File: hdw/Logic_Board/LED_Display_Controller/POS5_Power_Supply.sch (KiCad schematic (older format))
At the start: 15 parts, among them U401 LTC3624DD

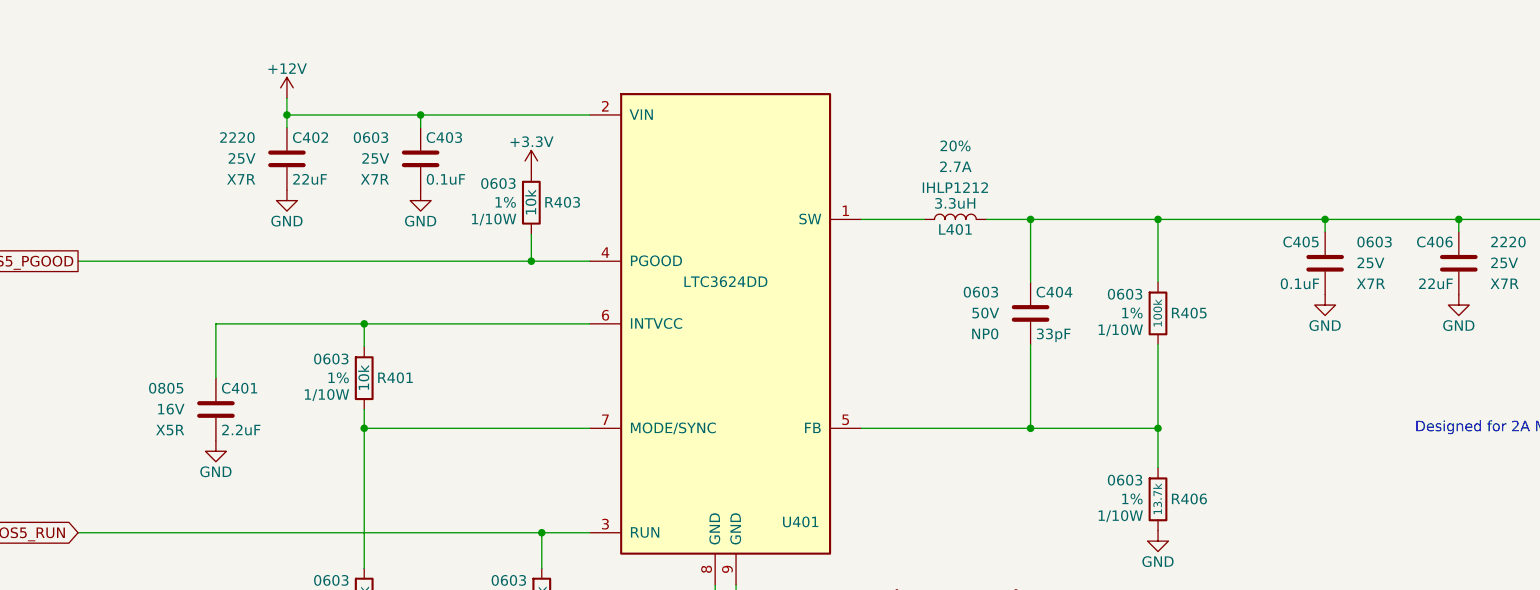
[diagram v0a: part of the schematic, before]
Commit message: Added some digikey partnumbers to components
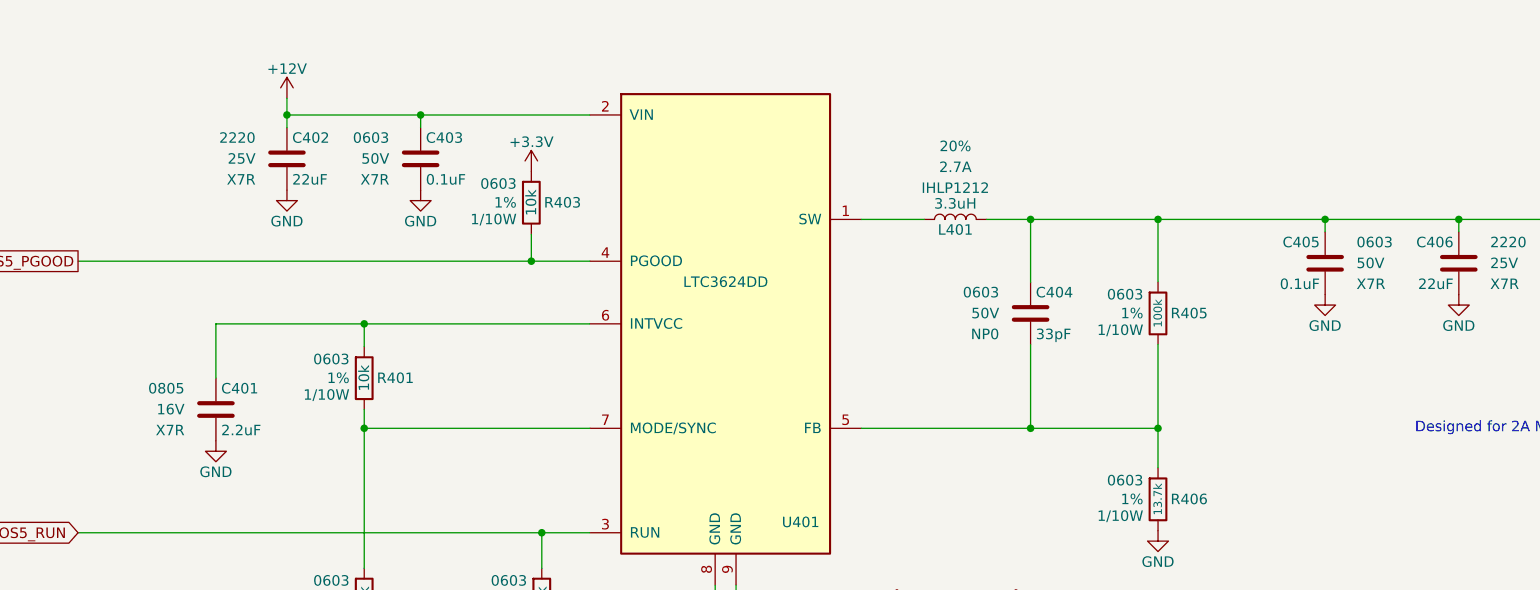
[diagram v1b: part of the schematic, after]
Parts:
- C401: Dielectric X5R -> X7R; Digi-Key PN PN -> 445-5691-1-ND
- C403, C405: footprint (none) -> Capacitors_SMD:C_0603; Digi-Key PN PN -> 311-1344-1-ND; Voltage 25V -> 50V
- C404: Digi-Key PN PN -> 399-1055-1-ND
- L401: Digi-Key PN (none) -> 541-2567-1-ND
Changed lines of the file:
@@
 F 5 "2.7A" V 6290 3230 50  0000 C CNN "Ampacity"
 F 6 "20%" V 6390 3230 50  0000 C CNN "Tolerance"
+F 7 "541-2567-1-ND" H 0   0   50  0001 C CNN "Digi-Key PN"
 	1    6040 3230
 	0    -1   -1   0
@@
 F 5 "50V" H 6250 3680 50  0000 R CNN "Voltage"
 F 6 "NP0" H 6250 3580 50  0000 R CNN "Dielectric"
-F 7 "PN" H 6825 4180 60  0001 C CNN "Digi-Key PN"
+F 7 "399-1055-1-ND" H 6825 4180 60  0001 C CNN "Digi-Key PN"
 	1    6400 3680
 	1    0    0    -1
@@
 F 4 "0805" H 2350 4240 50  0000 R CNN "display_footprint"
 F 5 "16V" H 2350 4140 50  0000 R CNN "Voltage"
-F 6 "X5R" H 2350 4040 50  0000 R CNN "Dielectric"
-F 7 "PN" H 2925 4640 60  0001 C CNN "Digi-Key PN"
+F 6 "X7R" H 2350 4040 50  0000 R CNN "Dielectric"
+F 7 "445-5691-1-ND" H 2925 4640 60  0001 C CNN "Digi-Key PN"
 	1    2500 4140
 	1    0    0    -1
@@
 F 0 "C405" H 7835 3540 50  0000 L CNN
 F 1 "0.1uF" H 7835 3340 50  0000 L CNN
-F 2 "" H 7848 3290 50  0001 C CNN
+F 2 "Capacitors_SMD:C_0603" H 7848 3290 50  0001 C CNN
 F 3 "" H 7835 3540 50  0001 C CNN
 F 4 "0603" H 7660 3540 50  0000 R CNN "display_footprint"
-F 5 "25V" H 7660 3440 50  0000 R CNN "Voltage"
+F 5 "50V" H 7660 3440 50  0000 R CNN "Voltage"
 F 6 "X7R" H 7660 3340 50  0000 R CNN "Dielectric"
-F 7 "PN" H 8235 3940 60  0001 C CNN "Digi-Key PN"
+F 7 "311-1344-1-ND" H 8235 3940 60  0001 C CNN "Digi-Key PN"
 	1    7810 3440
 	-1   0    0    -1
@@
 F 0 "C403" H 3505 3040 50  0000 L CNN
 F 1 "0.1uF" H 3505 2840 50  0000 L CNN
-F 2 "" H 3518 2790 50  0001 C CNN
+F 2 "Capacitors_SMD:C_0603" H 3518 2790 50  0001 C CNN
 F 3 "" H 3505 3040 50  0001 C CNN
 F 4 "0603" H 3330 3040 50  0000 R CNN "display_footprint"
-F 5 "25V" H 3330 2940 50  0000 R CNN "Voltage"
+F 5 "50V" H 3330 2940 50  0000 R CNN "Voltage"
 F 6 "X7R" H 3330 2840 50  0000 R CNN "Dielectric"
-F 7 "PN" H 3905 3440 60  0001 C CNN "Digi-Key PN"
+F 7 "311-1344-1-ND" H 3905 3440 60  0001 C CNN "Digi-Key PN"
 	1    3480 2940
 	1    0    0    -1

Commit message: Finished first pass of digikey part numbers
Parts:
- R401, R402, R403, R404: Digi-Key PN PN -> RMCF0603FT10K0CT-ND
- R405: Digi-Key PN PN -> A106046CT-ND
- R406: Digi-Key PN PN -> P13.7KHCT-ND
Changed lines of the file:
@@
 F 5 "1%" H 7080 3680 50  0000 L CNN "Tolerance"
 F 6 "1/10W" H 7080 3600 50  0000 L CNN "Wattage"
-F 7 "PN" H 7310 4080 60  0001 C CNN "Digi-Key PN"
+F 7 "A106046CT-ND" H 7310 4080 60  0001 C CNN "Digi-Key PN"
 	1    7010 3680
 	-1   0    0    -1
@@
 F 5 "1%" H 3280 3990 50  0000 L CNN "Tolerance"
 F 6 "1/10W" H 3280 3910 50  0000 L CNN "Wattage"
-F 7 "PN" H 3510 4390 60  0001 C CNN "Digi-Key PN"
+F 7 "RMCF0603FT10K0CT-ND" H 3510 4390 60  0001 C CNN "Digi-Key PN"
 	1    3210 3990
 	-1   0    0    -1
@@
 F 5 "1%" H 3280 5050 50  0000 L CNN "Tolerance"
 F 6 "1/10W" H 3280 4970 50  0000 L CNN "Wattage"
-F 7 "PN" H 3510 5450 60  0001 C CNN "Digi-Key PN"
+F 7 "RMCF0603FT10K0CT-ND" H 3510 5450 60  0001 C CNN "Digi-Key PN"
 	1    3210 5050
 	-1   0    0    -1
@@
 F 5 "1%" H 4130 5050 50  0000 L CNN "Tolerance"
 F 6 "1/10W" H 4130 4970 50  0000 L CNN "Wattage"
-F 7 "PN" H 4360 5450 60  0001 C CNN "Digi-Key PN"
+F 7 "RMCF0603FT10K0CT-ND" H 4360 5450 60  0001 C CNN "Digi-Key PN"
 	1    4060 5050
 	-1   0    0    -1
@@
 F 5 "1%" H 4080 3150 50  0000 L CNN "Tolerance"
 F 6 "1/10W" H 4080 3070 50  0000 L CNN "Wattage"
-F 7 "PN" H 4310 3550 60  0001 C CNN "Digi-Key PN"
+F 7 "RMCF0603FT10K0CT-ND" H 4310 3550 60  0001 C CNN "Digi-Key PN"
 	1    4010 3150
 	-1   0    0    -1
@@
 F 5 "1%" H 7080 4570 50  0000 L CNN "Tolerance"
 F 6 "1/10W" H 7080 4490 50  0000 L CNN "Wattage"
-F 7 "PN" H 7310 4970 60  0001 C CNN "Digi-Key PN"
+F 7 "P13.7KHCT-ND" H 7310 4970 60  0001 C CNN "Digi-Key PN"
 	1    7010 4570
 	-1   0    0    -1

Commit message: First pass assignment of footprints to all components
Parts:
- C401: footprint (none) -> Capacitors_SMD:C_0805
- C402, C406, C407: footprint (none) -> Capacitors_SMD:C_2220
- C404: footprint (none) -> Capacitors_SMD:C_0603
- L401: footprint (none) -> Inductors_SMD:L_Vishay_IHLP-1212
- R401, R402, R403, R404, R405, R406: footprint (none) -> Resistors_SMD:R_0603
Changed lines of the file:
@@
 F 0 "L401" V 5990 3230 50  0000 C CNN
 F 1 "3.3uH" V 6115 3230 50  0000 C CNN
-F 2 "" H 6040 3230 50  0001 C CNN
+F 2 "Inductors_SMD:L_Vishay_IHLP-1212" H 6040 3230 50  0001 C CNN
 F 3 "" H 6040 3230 50  0001 C CNN
 F 4 "IHLP1212" V 6190 3230 50  0000 C CNN "display_footprint"
@@
 F 0 "C404" H 6425 3780 50  0000 L CNN
 F 1 "33pF" H 6425 3580 50  0000 L CNN
-F 2 "" H 6438 3530 50  0001 C CNN
+F 2 "Capacitors_SMD:C_0603" H 6438 3530 50  0001 C CNN
 F 3 "" H 6425 3780 50  0001 C CNN
 F 4 "0603" H 6250 3780 50  0000 R CNN "display_footprint"
@@
 F 0 "R405" H 6950 3680 50  0000 R CNN
 F 1 "100k" V 7010 3680 40  0000 C CNN
-F 2 "" H 7010 3680 50  0001 C CNN
+F 2 "Resistors_SMD:R_0603" H 7010 3680 50  0001 C CNN
 F 3 "" H 7010 3680 50  0001 C CNN
 F 4 "0603" H 7080 3770 50  0000 L CNN "display_footprint"
@@
 F 0 "R401" H 3150 3990 50  0000 R CNN
 F 1 "10k" V 3210 3990 50  0000 C CNN
-F 2 "" H 3210 3990 50  0001 C CNN
+F 2 "Resistors_SMD:R_0603" H 3210 3990 50  0001 C CNN
 F 3 "" H 3210 3990 50  0001 C CNN
 F 4 "0603" H 3280 4080 50  0000 L CNN "display_footprint"
@@
 F 0 "R402" H 3150 5050 50  0000 R CNN
 F 1 "10k" V 3210 5050 50  0000 C CNN
-F 2 "" H 3210 5050 50  0001 C CNN
+F 2 "Resistors_SMD:R_0603" H 3210 5050 50  0001 C CNN
 F 3 "" H 3210 5050 50  0001 C CNN
 F 4 "0603" H 3280 5140 50  0000 L CNN "display_footprint"
@@
 F 0 "R404" H 4000 5050 50  0000 R CNN
 F 1 "10k" V 4060 5050 50  0000 C CNN
-F 2 "" H 4060 5050 50  0001 C CNN
+F 2 "Resistors_SMD:R_0603" H 4060 5050 50  0001 C CNN
 F 3 "" H 4060 5050 50  0001 C CNN
 F 4 "0603" H 4130 5140 50  0000 L CNN "display_footprint"
@@
 F 0 "C401" H 2525 4240 50  0000 L CNN
 F 1 "2.2uF" H 2525 4040 50  0000 L CNN
-F 2 "" H 2538 3990 50  0001 C CNN
+F 2 "Capacitors_SMD:C_0805" H 2538 3990 50  0001 C CNN
 F 3 "" H 2525 4240 50  0001 C CNN
 F 4 "0805" H 2350 4240 50  0000 R CNN "display_footprint"
@@
 F 0 "R403" H 3950 3150 50  0000 R CNN
 F 1 "10k" V 4010 3150 50  0000 C CNN
-F 2 "" H 4010 3150 50  0001 C CNN
+F 2 "Resistors_SMD:R_0603" H 4010 3150 50  0001 C CNN
 F 3 "" H 4010 3150 50  0001 C CNN
 F 4 "0603" H 4080 3240 50  0000 L CNN "display_footprint"
@@
 F 0 "C402" H 2865 3040 50  0000 L CNN
 F 1 "22uF" H 2865 2840 50  0000 L CNN
-F 2 "" H 2878 2790 50  0001 C CNN
+F 2 "Capacitors_SMD:C_2220" H 2878 2790 50  0001 C CNN
 F 3 "" H 2865 3040 50  0001 C CNN
 F 4 "445-1453-1-ND" H 3265 3440 60  0001 C CNN "Digi-Key PN"
@@
 F 0 "R406" H 6950 4570 50  0000 R CNN
 F 1 "13.7k" V 7010 4570 40  0000 C CNN
-F 2 "" H 7010 4570 50  0001 C CNN
+F 2 "Resistors_SMD:R_0603" H 7010 4570 50  0001 C CNN
 F 3 "" H 7010 4570 50  0001 C CNN
 F 4 "0603" H 7080 4660 50  0000 L CNN "display_footprint"
@@
 F 0 "C406" H 8475 3540 50  0000 L CNN
 F 1 "22uF" H 8475 3340 50  0000 L CNN
-F 2 "" H 8488 3290 50  0001 C CNN
+F 2 "Capacitors_SMD:C_2220" H 8488 3290 50  0001 C CNN
 F 3 "" H 8475 3540 50  0001 C CNN
 F 4 "445-1453-1-ND" H 8875 3940 60  0001 C CNN "Digi-Key PN"
@@
 F 0 "C407" H 9115 3540 50  0000 L CNN
 F 1 "22uF" H 9115 3340 50  0000 L CNN
-F 2 "" H 9128 3290 50  0001 C CNN
+F 2 "Capacitors_SMD:C_2220" H 9128 3290 50  0001 C CNN
 F 3 "" H 9115 3540 50  0001 C CNN
 F 4 "445-1453-1-ND" H 9515 3940 60  0001 C CNN "Digi-Key PN"

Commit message: Resolved a few library dependencies
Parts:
- R401, R402, R403, R404, R405, R406: symbol Custom_Library:R_Custom -> LED_Display_Local_Library:R_Custom
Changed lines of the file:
@@
 $EndComp
 $Comp
-L Custom_Library:R_Custom R405
+L LED_Display_Local_Library:R_Custom R405
 U 1 1 5BE635FD
 P 7010 3680
@@
 Connection ~ 4940 5020
 $Comp
-L Custom_Library:R_Custom R401
+L LED_Display_Local_Library:R_Custom R401
 U 1 1 5BE6F15A
 P 3210 3990
@@
 	4060 4730 4060 4900
 $Comp
-L Custom_Library:R_Custom R402
+L LED_Display_Local_Library:R_Custom R402
 U 1 1 5BE753C0
 P 3210 5050
@@
 $EndComp
 $Comp
-L Custom_Library:R_Custom R404
+L LED_Display_Local_Library:R_Custom R404
 U 1 1 5BE75409
 P 4060 5050
@@
 	3210 3730 2500 3730
 $Comp
-L Custom_Library:R_Custom R403
+L LED_Display_Local_Library:R_Custom R403
 U 1 1 5BE81C5D
 P 4010 3150
@@
 $EndComp
 $Comp
-L Custom_Library:R_Custom R406
+L LED_Display_Local_Library:R_Custom R406
 U 1 1 5BEEC3B4
 P 7010 4570
